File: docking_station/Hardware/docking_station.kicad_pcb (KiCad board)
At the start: 2 copper layers, 120 x 40 mm, 85 parts, among them IC1 VOM1271T, IC2 VOM1271T, IC3 VOM1271T, IC4 VOM1271T, IC5 VOM1271T, J1 WAGO, J2 XT60, J3 Conn_01x05_Pin, J5 SUPPLY+, J6 SUPPLY-, K1 RELPOL R40N-3021-85-1024, Q1 SIDR392DP-T1-GE3, Q10 DN2540N8-G, Q11 DN2540N8-G, Q12 2N7002K, Q2 SIDR392DP-T1-GE3, Q3 SIDR392DP-T1-GE3, Q4 SIDR392DP-T1-GE3, Q5 SIDR392DP-T1-GE3, Q6 SIDR392DP-T1-GE3, Q7 SIDR392DP-T1-GE3, Q8 SIDR392DP-T1-GE3, Q9 SIDR392DP-T1-GE3, U1 LTC4357MS8, U2 ACS712xLCTR-20A, U3 L78L05AB, U4 LMV321IYLT, U5 MCP6561T-E/OT, U6 MCP6561T-E/OT

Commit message: layout complete; footprint review complete
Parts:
- added R12: 10k, Resistor_SMD:R_0402_1005Metric, B.Cu at (139.4, 103.2)
- Q10, Q11: value DN2540N8-G -> 2N7002K; footprint Package_TO_SOT_SMD:SOT-89-3 -> Package_TO_SOT_SMD:SOT-23
- moved Q11 2.76 mm to (135.1, 111.1)
- moved GND3 1.75 mm to (126.0, 87.3)
- moved Q10 1.53 mm to (131.2, 111.1)
- moved TP9 0.61 mm to (130.2, 117.4)
- moved TP10 0.60 mm to (130.2, 91.7)
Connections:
- Q10 pad 1: Net-(Q10-D) -> Net-(IC5-A_2)
- Q10 pad 2: Net-(IC5-A_2) -> Net-(IC5-K_2)
- Q10 pad 3: Net-(IC5-K_2) -> Net-(Q10-D)
- Q11 pad 1: /LINE_A -> Net-(IC5-A_2)
- Q11 pad 2: Net-(IC5-A_2) -> Net-(IC5-K_2)
- Q11 pad 3: Net-(IC5-K_2) -> /LINE_A
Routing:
- net Net-(IC5-A_2): track 15.8 -> 11.2 mm
- net SENSE+: track 4.34 -> 7.08 mm, vias 10 -> 1
- net /LINE_A: track 56.9 -> 58.1 mm
- net Net-(IC5-K_2): track 8.69 -> 7.76 mm
- net SENSE-: track 4.91 -> 4.35 mm, vias 12 -> 0
- net GND: vias 232 -> 253
- net +24V: vias 33 -> 25
- removed copper zone on F.Cu, net SENSE+
- removed copper zone on F.Cu, net SENSE-
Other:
- board size 120 x 40 mm -> 120 x 43 mm

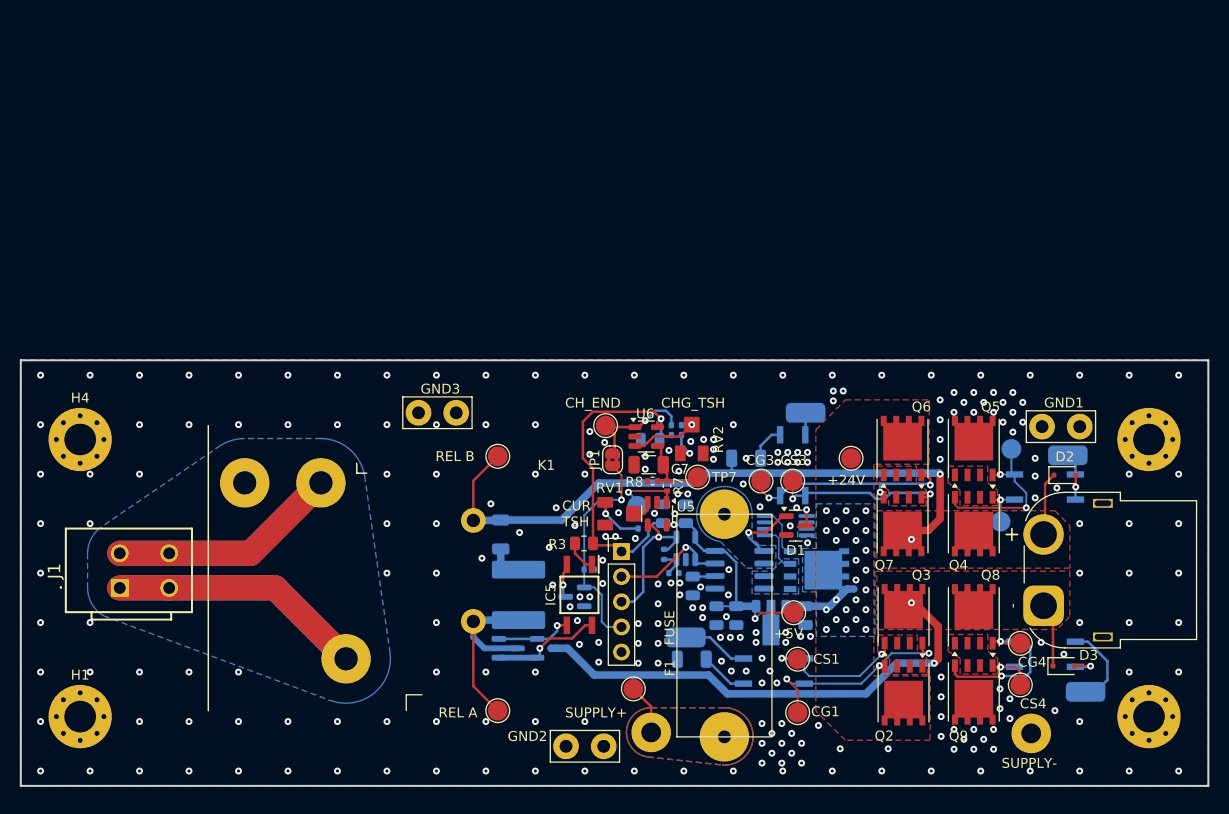
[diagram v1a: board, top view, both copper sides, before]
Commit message: docking station finished; 3d models & v_design added
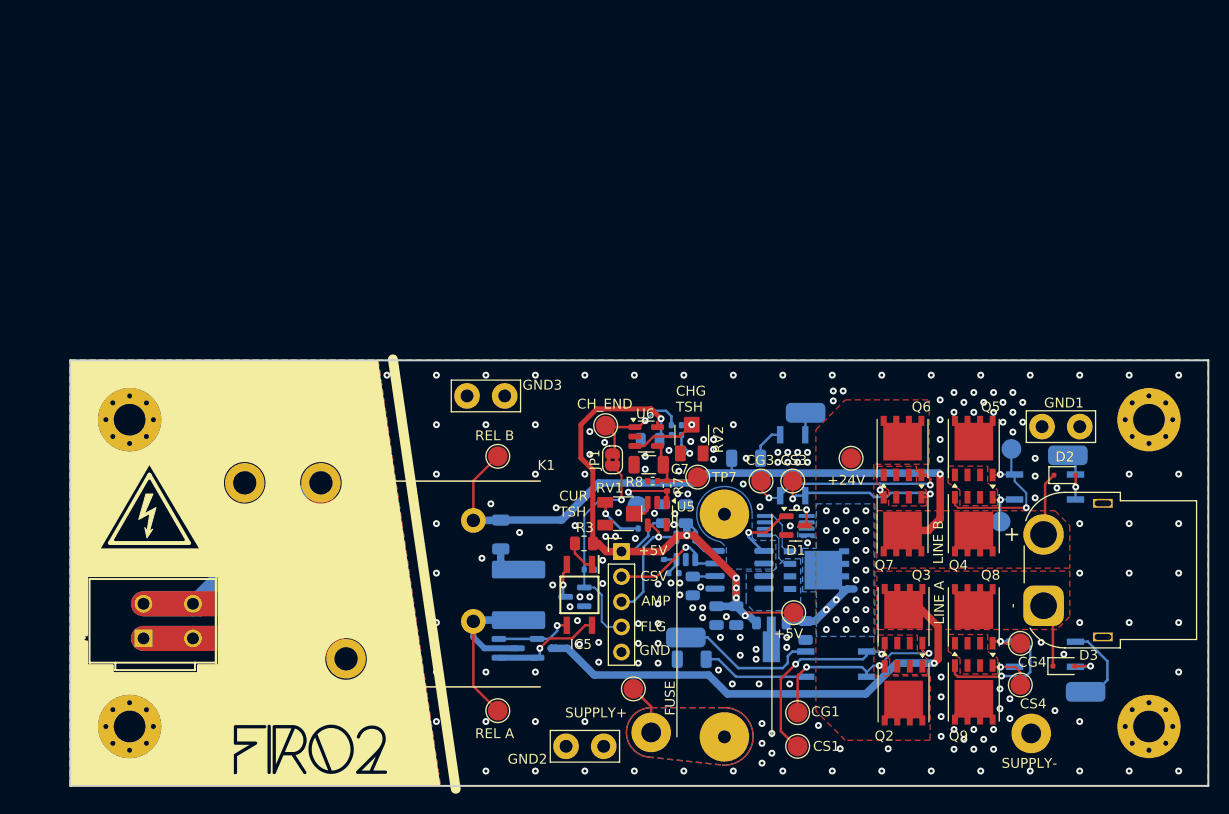
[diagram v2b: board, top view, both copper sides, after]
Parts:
- removed TP4, TP5: TestPoint, TestPoint:TestPoint_Pad_D2.0mm
- added REF**: Symbol_HighVoltage_Triangle_8x7mm_SScr, Symbol:Symbol_HighVoltage_Triangle_8x7mm_SScr, F.Cu at (95.0, 97.0)
- added REF**: FIRO2.1 (h=5mm) INV, firo_ID:FIRO2.1 (h=5mm) INV, F.Cu at (111.3, 121.3)
- added REF**: BLUE_boat_supersmall, BLUE_ID:BLUE_boat_supersmall, B.Cu at (178.1, 121.2)
- moved CS1 8.80 mm to (160.5, 121.0)
- moved IC1 6.34 mm to (164.4, 112.7)
- moved J1 5.64 mm to (99.4, 110.1)
- moved H4 5.39 mm to (93.0, 88.0)
- moved GND3 5.19 mm to (130.9, 85.6)
- moved H1 5.10 mm to (93.0, 119.0)
- moved H3 2.00 mm to (196.0, 88.0)
- moved U3 1.70 mm to (157.8, 110.5)
- moved C2 1.50 mm to (161.3, 109.3)
- moved H2 1.00 mm to (196.0, 119.0)
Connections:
- H1 pad 1: GND -> unconnected-(H1-Pad1)_7
- H4 pad 1: GND -> unconnected-(H4-Pad1)_2
- Q11 pad 3: /LINE_A -> Net-(IC1-A_2)
- Q3 pad 3: /LINE_A -> Net-(IC1-A_2)
- R1 pad 2: /LINE_A -> Net-(IC1-A_2)
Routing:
- net /LINE_A: track 58.1 -> 6.49 mm, vias 2 -> 0
- net Net-(IC1-A_2): track 21.8 -> 72.9 mm, vias 3 -> 4
- net +5V: track 59.5 -> 73.7 mm, vias 3 -> 7
- net Net-(J1-Pin_1): track 51.7 -> 42.6 mm
- net Net-(CJ1-Pin_1): track 6.71 -> 14.5 mm
- net Net-(IC1-A_1): track 4.79 -> 10.8 mm
- net /CS_1: track 15.4 -> 20.5 mm
- net Net-(J1-Pin_2): track 46.6 -> 48.8 mm
- net +24V: track 7.62 -> 8.28 mm
- net GND: vias 253 -> 192
- net /LINE_B: vias 2 -> 1
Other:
- board size 120 x 43 mm -> 115 x 43 mm
- board text added: "AMP"
- board text added: "CHG TSH"
- board text added: "CSV"
- board text added: "FIRO 2.1 ('24) Docking Station v1, 26.07 PU"
- board text added: "FLG"
- board text added: "GND"
- board text added: "SOLDER THE CABLE JUMPERS BEFORE OPERATION"
- board text removed: "CHG_TSH"

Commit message: Readability update begin
Added LEDs
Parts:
- removed GND3: TestPoint, TestPoint:TestPoint_Bridge_Pitch3.81mm_Drill1.3mm
- added D10: RB560VM-40TE-17, Diode_SMD:D_SOD-323F, F.Cu at (126.8, 61.3)
- added D4: LED, LED_SMD:LED_0805_2012Metric, F.Cu at (118.0, 50.3)
- added D5: LED, LED_SMD:LED_0805_2012Metric, F.Cu at (118.0, 53.4)
- added D6: LED, LED_SMD:LED_0805_2012Metric, F.Cu at (118.0, 56.4)
- added D7: LED, LED_SMD:LED_0805_2012Metric, F.Cu at (118.0, 59.4)
- added D8: LED, LED_SMD:LED_0805_2012Metric, F.Cu at (118.0, 62.5)
- added D9: RB560VM-40TE-17, Diode_SMD:D_SOD-323F, F.Cu at (126.8, 58.4)
- added R13: R, Resistor_SMD:R_0805_2012Metric, F.Cu at (122.5, 50.3)
- added R14: R, Resistor_SMD:R_0805_2012Metric, F.Cu at (122.5, 53.2)
- added R15: R, Resistor_SMD:R_0805_2012Metric, F.Cu at (122.5, 56.2)
- added R16: R, Resistor_SMD:R_0805_2012Metric, F.Cu at (122.5, 59.1)
- added R17: R, Resistor_SMD:R_0805_2012Metric, F.Cu at (122.5, 62.1)
- moved GND2 37.5 mm to (126.9, 86.2), turned to 0 degrees
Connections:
- net CH_END renamed CHARGING
- Q11 pad 3: Net-(IC1-A_2) -> /LINE_A
- Q3 pad 3: Net-(IC1-A_2) -> /LINE_A
- R1 pad 2: Net-(IC1-A_2) -> /LINE_A
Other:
- board text added: "TO CJ1"
- board text added: "TO CJ2"
- board text added: "TO CJ3"
- board text added: "TO CJ4"

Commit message: PCB layout, design and BOM complete; pending review
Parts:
- removed D10, D9: RB560VM-40TE-17, Diode_SMD:D_SOD-323F
- removed D7, D8: LED, LED_SMD:LED_0805_2012Metric
- added C10: 100nF, Capacitor_SMD:C_0805_2012Metric, B.Cu at (131.9, 94.3)
- added D11: B3V1, LED_SMD:LED_0805_2012Metric, F.Cu at (192.1, 93.2)
- added D12: B3V1, LED_SMD:LED_0805_2012Metric, F.Cu at (192.1, 113.2)
- added JP2: Jumper_2_Small_Bridged, Jumper:SolderJumper-2_P1.3mm_Bridged2Bar_RoundedPad1.0x1.5mm, B.Cu at (138.4, 93.1)
- added Q13: 2N7002K, Package_TO_SOT_SMD:SOT-23, B.Cu at (135.8, 94.9)
- added R18: 10k, Resistor_SMD:R_0402_1005Metric, B.Cu at (132.0, 89.4)
- added R19: 1k5, Resistor_SMD:R_0402_1005Metric, B.Cu at (136.1, 92.0)
- added R20: 150k, Resistor_SMD:R_0402_1005Metric, B.Cu at (130.9, 91.0)
- added TH1: Thermistor, Resistor_THT:R_Axial_DIN0204_L3.6mm_D1.6mm_P2.54mm_Vertical, B.Cu at (136.1, 89.4)
- added U7: MCP6561T-E/OT, Package_TO_SOT_SMD:SOT-23-5, B.Cu at (133.5, 91.6)
- C4, C5, C6, C8: value 10nF -> 100nF
- C9: value 22uF -> 47uF
- D4, D5: value LED -> G2V4
- D6: value LED -> B3V1
- J2: footprint Connector_AMASS:AMASS_XT60PW-F_1x02_P7.20mm_Horizontal -> firo_footprints:AMASS_XT60PW-F-MP
- R1, R2: value 1k3 -> 1k2
- R11: value 1k -> 240; footprint Resistor_SMD:R_1206_3216Metric -> Resistor_SMD:R_0805_2012Metric
- R12: value 10k -> 15k
- R13: value R -> 2k2; footprint Resistor_SMD:R_0805_2012Metric -> Resistor_SMD:R_1206_3216Metric
- R14, R15: value R -> 240; moved to B.Cu
- R16: value R -> 1k; footprint Resistor_SMD:R_0805_2012Metric -> Resistor_SMD:R_0402_1005Metric
- R17: value R -> 10k; footprint Resistor_SMD:R_0805_2012Metric -> Resistor_SMD:R_0402_1005Metric; moved to B.Cu
- R3: value 170 -> 240
- moved D6 60.8 mm to (139.1, 113.4), turned to 90 degrees
- moved D4 56.5 mm to (159.5, 88.7), turned to -90 degrees
- moved R15 56.3 mm to (139.1, 110.0), turned to -90 degrees
- moved R13 56.2 mm to (162.7, 89.5), turned to 180 degrees
- moved D5 52.2 mm to (156.5, 88.7), turned to -90 degrees
- moved R14 45.0 mm to (151.2, 87.9), turned to -90 degrees
- moved R16 36.2 mm to (142.5, 89.3), turned to 90 degrees
- moved R17 29.6 mm to (133.9, 89.4), turned to 180 degrees
- moved GND2 2.40 mm to (124.5, 86.0)
- moved TP8 1.82 mm to (139.3, 88.9)
- moved TP2 1.08 mm to (165.3, 92.8)
- moved RV1 0.15 mm to (142.3, 97.5)
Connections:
- D2 pad 2: Net-(D2-A) -> Net-(D11-K)
- D3 pad 2: Net-(D3-A) -> Net-(D12-K)
- IC2 pad 2: Net-(D2-A) -> Net-(D11-A)
- IC4 pad 2: Net-(D3-A) -> Net-(D12-A)
- R10 pad 2: Net-(JP1-A) -> FLAG_LED
- R15 pad 1: CHARGING -> FLAG_LED
- R16 pad 1: /LINE_A -> Net-(JP1-A)
- R16 pad 2: Net-(D7-A) -> FLAG_LED
- R17 pad 1: /LINE_B -> +5V
- TP8 pad 1: Net-(JP1-A) -> FLAG_LED
- U6 pad 1: Net-(JP1-A) -> FLAG_LED
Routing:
- net Net-(IC1-A_2): track 72.9 -> 20.7 mm, vias 4 -> 3
- net FLAG_LED: track 0.00 -> 52.0 mm, vias 0 -> 2
- net /LINE_A: track 6.49 -> 58.1 mm, vias 0 -> 1
- net +5V: track 73.7 -> 92.6 mm, vias 7 -> 9
- net Net-(JP1-A): track 11.8 -> 2.17 mm, vias 1 -> 0
- net Net-(Q13-G): track 0.00 -> 7.91 mm
- net Net-(D5-A): track 0.00 -> 5.69 mm, vias 0 -> 1
- net Net-(D11-A): track 0.00 -> 5.05 mm, vias 0 -> 1
- net Net-(D12-K): track 0.00 -> 4.11 mm
- net Net-(D11-K): track 0.00 -> 4.05 mm
- net Net-(U7-+): track 0.00 -> 3.85 mm
- net Net-(D12-A): track 0.00 -> 3.82 mm, vias 0 -> 1
- net Net-(U7--): track 0.00 -> 3.46 mm
- net Net-(D3-A): track 3.15 -> 0.00 mm, vias 1 -> 0
- net CHARGING: track 22.5 -> 25.4 mm, vias 1 -> 2
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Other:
- board text added: "24V"
- board text added: "CHG"
- board text added: "JP1: CURRENT FLAG JP2: THERMAL FLAG"
- board text added: "JUMPERS"
- board text added: "OUT1"
- board text added: "TEMP"

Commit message: File structure & documentation
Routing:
- net GND: vias 189 -> 185
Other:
- board text added: "#"
- board text added: "T PROBE"
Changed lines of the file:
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@@
 		(allow_soldermask_bridges_in_footprints no)
 		(pcbplotparams
-			(layerselection 0x00010fc_ffffffff)
+			(layerselection 0x0001020_7fffffff)
 			(plot_on_all_layers_selection 0x0000000_00000000)
 			(disableapertmacros no)
@@
 			(svgprecision 4)
 			(plotframeref no)
-			(viasonmask no)
+			(viasonmask yes)
 			(mode 1)
 			(useauxorigin no)
@@
 			(pdf_back_fp_property_popups yes)
 			(dxfpolygonmode yes)
-			(dxfimperialunits yes)
+			(dxfimperialunits no)
 			(dxfusepcbnewfont yes)
 			(psnegative no)
 			(psa4output no)
-			(plotreference yes)
-			(plotvalue yes)
-			(plotfptext yes)
+			(plotreference no)
+			(plotvalue no)
+			(plotfptext no)
 			(plotinvisibletext no)
 			(sketchpadsonfab no)
 			(subtractmaskfromsilk no)
-			(outputformat 1)
+			(outputformat 3)
 			(mirror no)
-			(drillshape 1)
+			(drillshape 0)
 			(scaleselection 1)
 			(outputdirectory "")
@@
 		(tags "SOT TO_SOT_SMD")
 		(property "Reference" "D1"
-			(at 0 2.5 0)
+			(at 1.45 -2.7 0)
 			(layer "F.SilkS")
 			(effects
@@
 			(layer "F.Fab")
 		)
-		(fp_text user "+"
-			(at -6.3 3.15 -90)
+		(fp_text user "-"
+			(at -0.7 3.05 -90)
 			(layer "F.SilkS")
 			(effects
 				(font
-					(size 1.5 1.5)
+					(size 1 1)
 					(thickness 0.15)
 				)
 			)
 		)
-		(fp_text user "-"
-			(at -0.7 3.05 -90)
+		(fp_text user "+"
+			(at -6.3 3.15 -90)
 			(layer "F.SilkS")
 			(effects
 				(font
-					(size 1 1)
+					(size 1.5 1.5)
 					(thickness 0.15)
 				)
@@
 			(pintype "passive")
 		)
-		(model "${KICAD8_3DMODEL_DIR}/Connector_AMASS.3dshapes/AMASS_XT60PW-F_1x02_P7.20mm_Horizontal.wrl"
+		(model "${KIPRJMOD}/3dmodels/XT60PW-F.stp"
 			(offset
-				(xyz 0 0 0)
+				(xyz -3.6 0 0)
 			)
 			(scale
@@
 			)
 			(rotate
-				(xyz 0 0 0)
+				(xyz 90 180 0)
 			)
 		)
@@
 	)
 	(gr_text "OUT1"
-		(at 146.1 94.9 0)
+		(at 142.8 94.7 90)
 		(layer "B.SilkS")
 		(effects
@@
 		)
 	)
+	(gr_text "T PROBE"
+		(at 158.5 105.3 0)
+		(layer "F.SilkS" knockout)
+		(effects
+			(font
+				(size 1 1)
+				(thickness 0.1)
+			)
+			(justify left bottom)
+		)
+	)
 	(gr_text "CH_END\n"
 		(at 137.1 87.2 0)
@@
 		)
 	)
+	(gr_text "#"
+		(at 133.5 122.8 0)
+		(layer "F.SilkS" knockout)
+		(effects
+			(font
+				(size 1 1)
+				(thickness 0.15)
+			)
+			(justify left bottom)
+		)
+	)
 	(gr_text "AMP"
 		(at 144.7 106.9 0)
@@
 	)
 	(via
-		(at 180.3 87.25)
-		(size 0.7)
-		(drill 0.3)
-		(layers "F.Cu" "B.Cu")
-		(free yes)
-		(net 2)
-	)
-	(via
 		(at 148.6 104.5)
 		(size 0.7)
@@
 	)
 	(via
-		(at 176.3 119.3)
-		(size 0.7)
-		(drill 0.3)
-		(layers "F.Cu" "B.Cu")
-		(free yes)
-		(net 2)
-	)
-	(via
 		(at 148.4 95.5)
 		(size 0.7)
@@
 	)
 	(via
-		(at 179.3 86.25)
-		(size 0.7)
-		(drill 0.3)
-		(layers "F.Cu" "B.Cu")
-		(free yes)
-		(net 2)
-	)
-	(via
 		(at 174.9 86)
 		(size 0.7)
@@
 	)
 	(via
-		(at 177.3 120.3)
-		(size 0.7)
-		(drill 0.3)
-		(layers "F.Cu" "B.Cu")
-		(free yes)
-		(net 2)
-	)
-	(via
 		(at 129 83.5)
 		(size 0.7)
@@
 		(min_thickness 0.25)
 		(filled_areas_thickness no)
+		(fill yes
+			(mode hatch)
+			(thermal_gap 0.5)
+			(thermal_bridge_width 0.5)
+			(hatch_thickness 0.25)
+			(hatch_gap 1)
+			(hatch_orientation 45)
+			(hatch_border_algorithm hatch_thickness)
+			(hatch_min_hole_area 0.3)
+		)
+		(polygon
+			(pts
+				(xy 158.15 101.1) (xy 165.35 101.1) (xy 165.35 105.35) (xy 165 105.35) (xy 165 104.1) (xy 158.5 104.1)
+				(xy 158.5 105.35) (xy 158.15 105.35)
+			)
+		)
+	)
+	(zone
+		(net 0)
+		(net_name "")
+		(layer "F.SilkS")
+		(hatch edge 0.5)
+		(connect_pads
+			(clearance 0)
+		)
+		(min_thickness 0.25)
+		(filled_areas_thickness no)
+		(fill yes
+			(thermal_gap 0.5)
+			(thermal_bridge_width 0.5)
+		)
+		(polygon
+			(pts
+				(xy 133.5 118) (xy 139.5 118) (xy 139.5 124) (xy 133.5 124)
+			)
+		)
+	)
+	(zone
+		(net 0)
+		(net_name "")
+		(layer "F.SilkS")
+		(hatch edge 0.5)
+		(connect_pads
+			(clearance 0)
+		)
+		(min_thickness 0.25)
+		(filled_areas_thickness no)
 		(keepout
 			(tracks allowed)
@@
 			)
 		)
+	)
+	(zone
+		(net 0)
+		(net_name "")
+		(layer "F.SilkS")
+		(hatch edge 0.5)
+		(connect_pads
+			(clearance 0)
+		)
+		(min_thickness 0.25)
+		(filled_areas_thickness no)
+		(keepout
+			(tracks not_allowed)
+			(vias not_allowed)
+			(pads not_allowed)
+			(copperpour allowed)
+			(footprints allowed)
+		)
+		(fill
+			(mode hatch)
+			(thermal_gap 0.5)
+			(thermal_bridge_width 0.5)
+			(hatch_thickness 0.25)
+			(hatch_gap 1)
+			(hatch_orientation 45)
+			(hatch_border_algorithm hatch_thickness)
+			(hatch_min_hole_area 0.3)
+		)
+		(polygon
+			(pts
+				(xy 133.6 123) (xy 133.612952 121.450015) (xy 134.612952 121.450015) (xy 134.6 123)
+			)
+		)

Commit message: i_hate_git_please_end_this
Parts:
- added R3: 10k, Resistor_SMD:R_0402_1005Metric, B.Cu at (150.4, 102.5)
- added R4: 100k, Resistor_SMD:R_0402_1005Metric, B.Cu at (148.4, 104.4)
- added R6: 4k7, Resistor_SMD:R_0402_1005Metric, B.Cu at (145.6, 105.1)
- added R8: 100k, Resistor_SMD:R_0402_1005Metric, B.Cu at (146.1, 102.6)
- C7: value 47u -> 100u
- R17: renamed from R12; value 15k -> 68k
- R5: value 100k -> 4k7
- R7: renamed from R4; value 1k -> 10k
- moved R7 2.47 mm to (145.6, 104.1), turned to 180 degrees
- moved R5 2.13 mm to (145.1, 102.6)
- moved U4 1.10 mm to (148.2, 101.3)
- moved C4 0.35 mm to (149.9, 105.2)
- renumbered C2 to C1, C3 to C2, C6 to C3, C1 to C4, C4 to C5, C5 to C6, D11 to D3, D3 to D4, D12 to D5, D4 to D6, D5 to D7, D6 to D8, H4 to H3, H3 to H4, J5 to J1, J6 to J2, J2 to J4, J1 to J5, Q12 to Q11, Q11 to Q12, R7 to R10, R8 to R11, R9 to R12, R10 to R13, R16 to R14, R11 to R15, R3 to R16, R17 to R18, R18 to R20, R20 to R21, R13 to R22, R14 to R23, R15 to R24, R6 to R9, TP6 to TP2, TP7 to TP3, TP8 to TP4, TP9 to TP5, TP10 to TP6, TP2 to TP7, TP3 to TP8, U3 to U2, U2 to U3
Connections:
- J3 pad 2: /CS_VOUT -> /AMP_OUT
- J3 pad 3: /AMP_OUT -> GND
- R5 pad 1: Net-(U4--) -> Net-(R5-Pad1)
- R5 pad 2: /AMP_OUT -> +5V
- R7 pad 2: GND -> Net-(R5-Pad1)
- U4 pad 1: /CS_VOUT -> Net-(U4-+)
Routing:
- net /CS_VOUT: track 11.8 -> 1.95 mm, vias 1 -> 0
- net /AMP_OUT: track 14.8 -> 10.7 mm
- net Net-(U4-+): track 0.00 -> 3.50 mm
- net Net-(R5-Pad1): track 0.00 -> 1.98 mm
- net +5V: track 92.6 -> 93.9 mm
- net GND: track 0.00 -> 0.07 mm, vias 185 -> 176
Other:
- board text removed: "CSV"

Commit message: update
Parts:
- renumbered R7 to R10, R6 to R11, R8 to R6, R11 to R7, R10 to R8
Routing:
- net GND: vias 176 -> 183
- net +24V: vias 25 -> 15

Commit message: a lot of work done
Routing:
- net +5V: track 93.9 -> 95.2 mm
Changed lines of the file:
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@@
+	)
+	(segment
+		(start 153.5 101)
+		(end 154.3 101.8)
+		(width 0.762)
+		(layer "F.Cu")
+		(net 3)
 	)
 	(segment
@@
 	)
 	(segment
-		(start 148.4 99.7)
-		(end 150 99.7)
-		(width 0.762)
+		(start 148 98.6)
+		(end 147.2875 98.6)
+		(width 0.254)
 		(layer "F.Cu")
 		(net 3)
 	)
 	(segment
-		(start 148 98.6)
-		(end 147.2875 98.6)
-		(width 0.254)
+		(start 154.3 101.8)
+		(end 154.3 104)
+		(width 0.762)
 		(layer "F.Cu")
 		(net 3)
@@
 	)
 	(segment
-		(start 150 99.7)
-		(end 154.3 104)
+		(start 151 101)
+		(end 153.5 101)
+		(width 0.762)
+		(layer "F.Cu")
+		(net 3)
+	)
+	(segment
+		(start 148.4 99.7)
+		(end 149.7 99.7)
 		(width 0.762)
 		(layer "F.Cu")
@@
 		(width 0.762)
 		(layer "F.Cu")
+		(net 3)
+	)
+	(segment
+		(start 149.7 99.7)
+		(end 151 101)
+		(width 0.762)
+		(layer "F.Cu")
